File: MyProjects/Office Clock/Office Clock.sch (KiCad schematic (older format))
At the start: 14 parts, among them M1 DLX3416, M2 DLX3416, Q1 Q_Photo_NPN_CE, U1 MAX7219, U2 D1_Mini, U3 74HCT367N, U4 74HCT164N

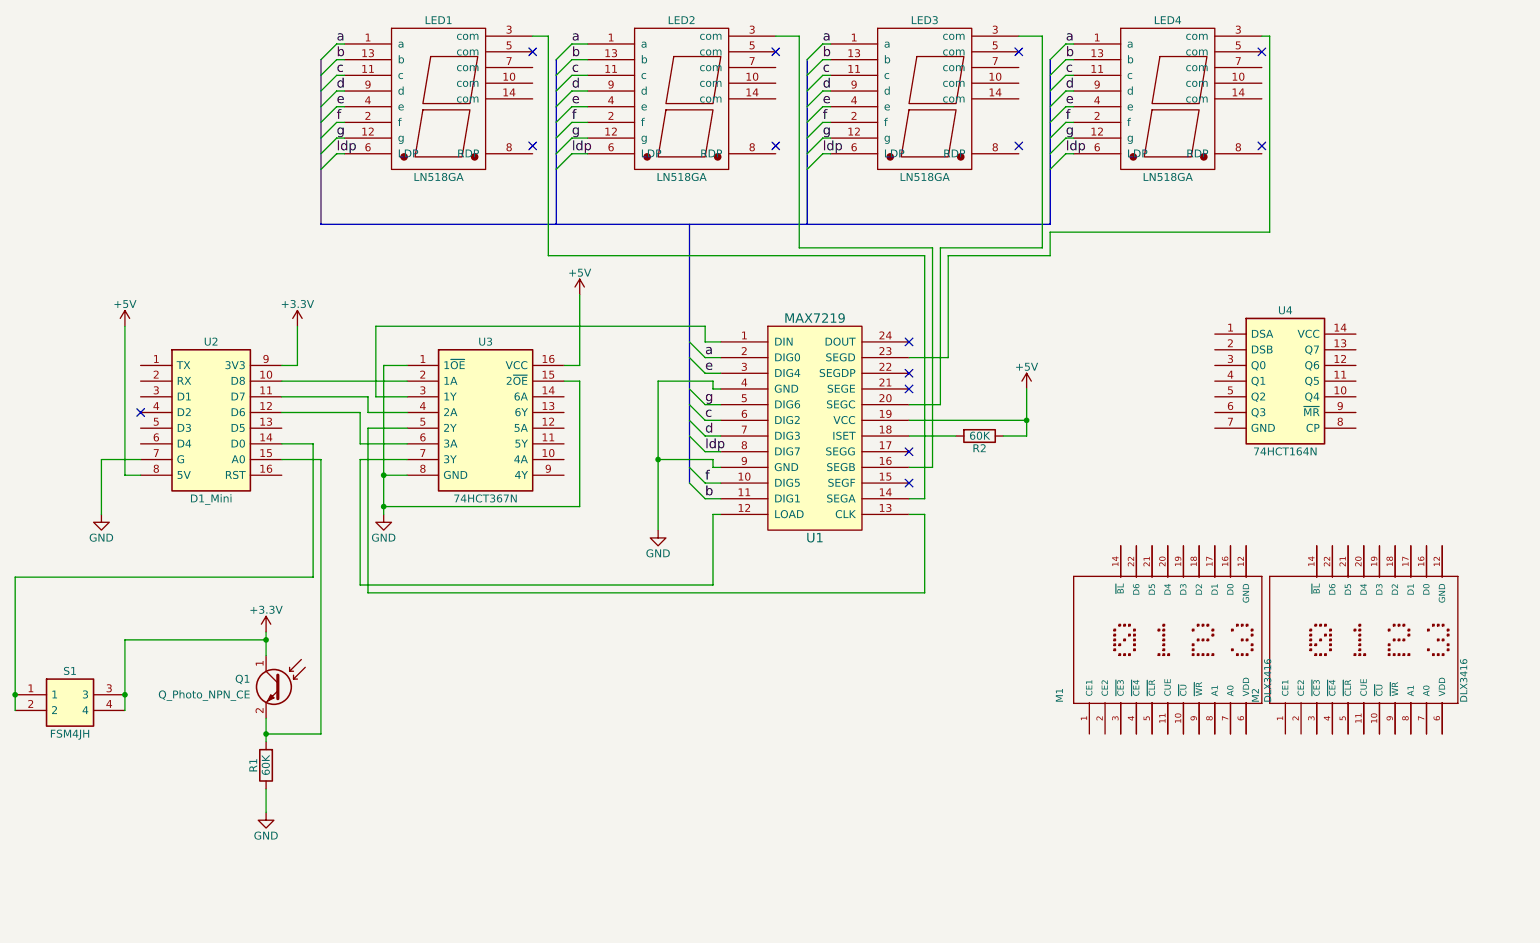
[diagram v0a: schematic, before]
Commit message: Finished schematic wiring
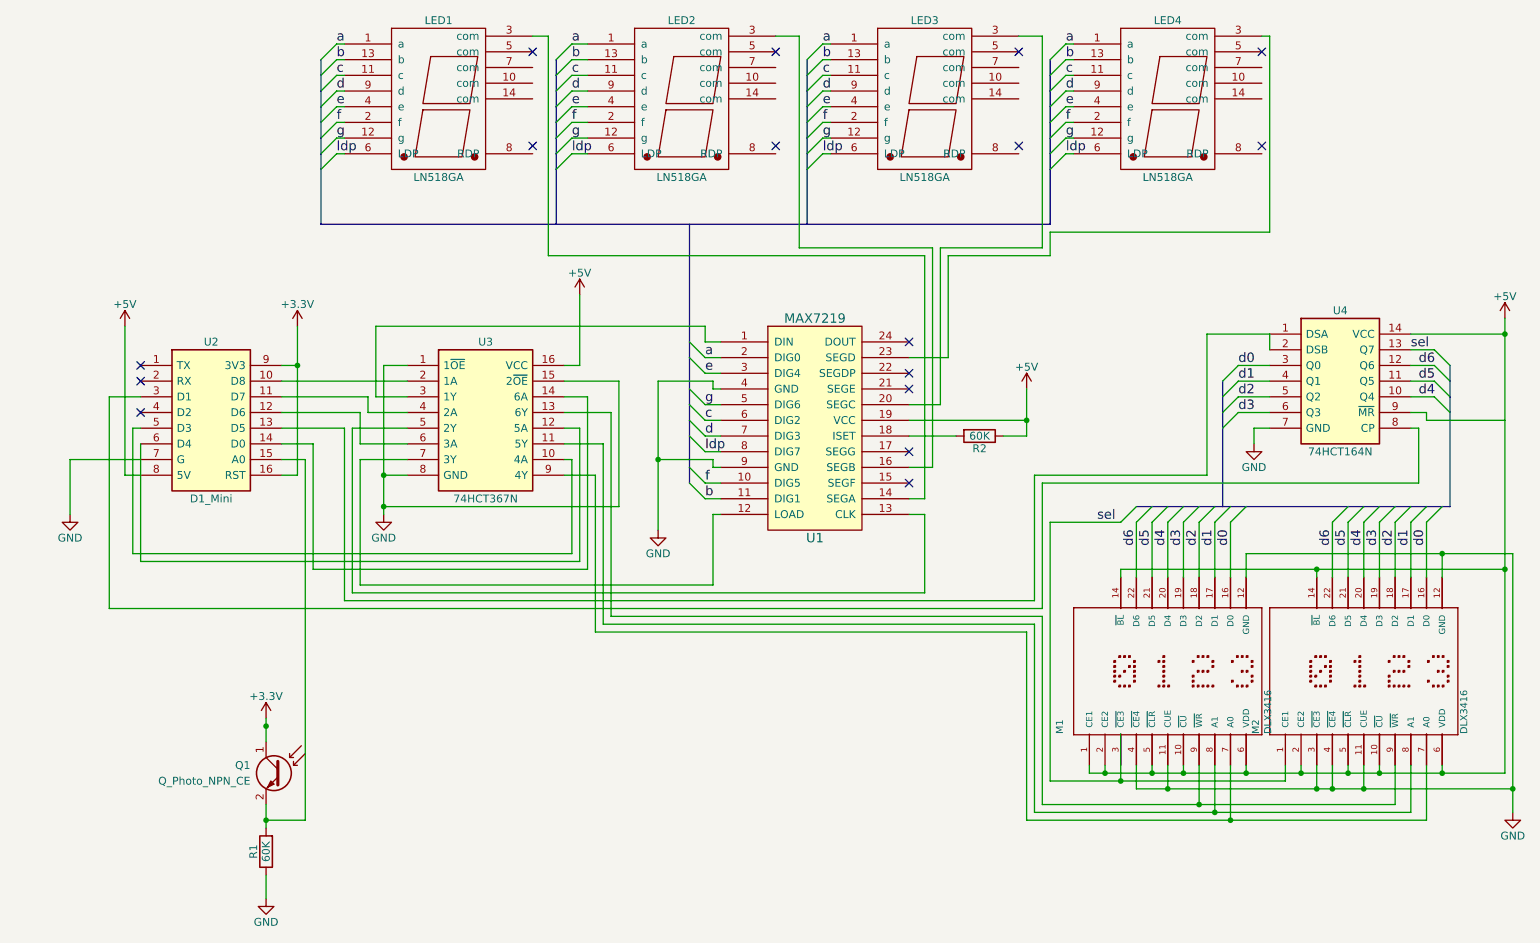
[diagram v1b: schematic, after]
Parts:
- removed S1: FSM4JH, FSM4JH, symbol FSM4JH
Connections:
- net +3V3: now also U2.16 (RST)
- net +5V: now also M1.1 (CE1), M1.10 (~CU), M1.14 (~BL), M1.2 (CE2), M1.5 (~CLR), M1.6 (VDD), M2.10 (~CU), M2.14 (~BL), M2.2 (CE2), M2.5 (~CLR), M2.6 (VDD), U4.14 (VCC)
- net GND: now also M1.11 (CUE), M1.12 (GND), M1.4 (~CE4), M2.11 (CUE), M2.12 (GND), M2.3 (~CE3), M2.4 (~CE4), U4.7 (GND)
- net at U3.10 (4A): now also U2.5 (D3)
- net at U3.11 (5Y): now also M1.8 (A1), M2.8 (A1)
- net at U3.12 (5A): now also U2.6 (D4)
- net at U3.13 (6Y): now also M1.9 (~WR), M2.9 (~WR)
- net at U3.14 (6A): now also U2.14 (D0)
- net at U3.9 (4Y): now also M1.7 (A0), M2.7 (A0)
- net at U2.13 (D5): now also U4.1 (DSA), U4.2 (DSB)
- net at U2.3 (D1): now also U4.8 (CP)
- net d0: now reaches M1.16 (D0)
- net d0: now also M2.16 (D0), U4.3 (Q0)
- net d1: now reaches M1.17 (D1)
- net d1: now also M2.17 (D1), U4.4 (Q1)
- net d2: now reaches M1.18 (D2)
- net d2: now also M2.18 (D2), U4.5 (Q2)
- net d3: now reaches M1.19 (D3)
- net d3: now also M2.19 (D3), U4.6 (Q3)
- net d4: now reaches M1.20 (D4)
- net d4: now also M2.20 (D4), U4.10 (Q4)
- net d5: now reaches M1.21 (D5)
- net d5: now also M2.21 (D5), U4.11 (Q5)
- net d6: now reaches M1.22 (D6)
- net d6: now also M2.22 (D6), U4.12 (Q6)
- net sel: now reaches M2.1 (CE1)
- net sel: now also U4.13 (Q7)
- no-connect marks 14 -> 16
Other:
- moved on the sheet: M1, M2, Q1, R1, U4

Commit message: Finished laying out board with filled zones
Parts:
- removed LED1, LED2, LED3, LED4: LN518GA, LN518xx:LN518xx, symbol LN518xx
- added AFF1, AFF2, AFF3, AFF4: LN518xx, LN518xx:LN518xx, symbol LN518xx
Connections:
- net a: now also AFF1.1 (a), AFF2.1 (a), AFF3.1 (a), AFF4.1 (a)
- net b: now also AFF1.13 (b), AFF2.13 (b), AFF3.13 (b), AFF4.13 (b)
- net c: now also AFF1.11 (c), AFF2.11 (c), AFF3.11 (c), AFF4.11 (c)
- net d: now also AFF1.9 (d), AFF2.9 (d), AFF3.9 (d), AFF4.9 (d)
- net e: now also AFF1.4 (e), AFF2.4 (e), AFF3.4 (e), AFF4.4 (e)
- net f: now also AFF1.2 (f), AFF2.2 (f), AFF3.2 (f), AFF4.2 (f)
- net g: now also AFF1.12 (g), AFF2.12 (g), AFF3.12 (g), AFF4.12 (g)
- net ldp: now also AFF1.6 (LDP), AFF2.6 (LDP), AFF3.6 (LDP), AFF4.6 (LDP)
- net sel: now also M1.3 (~CE3)
- net at U1.14 (SEGA): now also AFF1.3 (com)
- net at U1.16 (SEGB): now also AFF2.3 (com)
- net at U1.20 (SEGC): now also AFF3.3 (com)
- net at U1.23 (SEGD): now also AFF4.3 (com)
- net at U3.2 (1A): now also U2.12 (D6); no longer U2.10 (D8)
- net at U3.6 (3A): now also U2.10 (D8); no longer U2.12 (D6)
- no-connect marks 16 -> 28
